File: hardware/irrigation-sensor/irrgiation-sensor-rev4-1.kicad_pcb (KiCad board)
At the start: 2 copper layers, 180 x 38 mm, 39 parts, among them J1 CONUFL001-SMD-T, J2 SHF-105-01-L-D-TH, Q1 TSM260P02, Q2 PMV250EPEA, U1 24LC32, U2 RFM95W, U3 STM32L412KB, U4 TLV61225, Y1 32768Hz

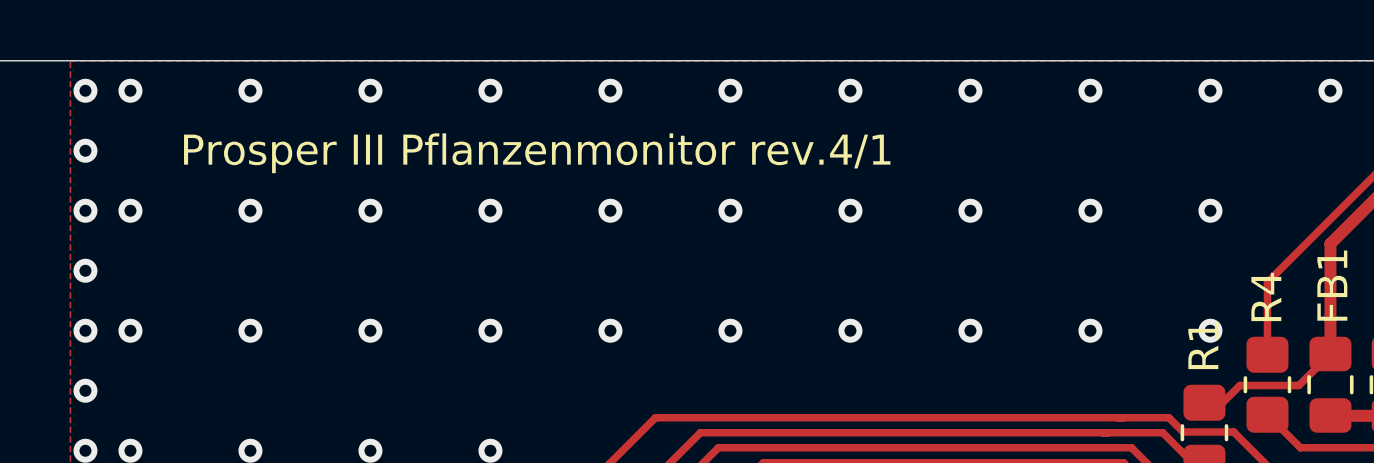
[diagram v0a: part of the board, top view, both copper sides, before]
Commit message: Add different irrigation sensor hardware revisions and cypress e2e tests
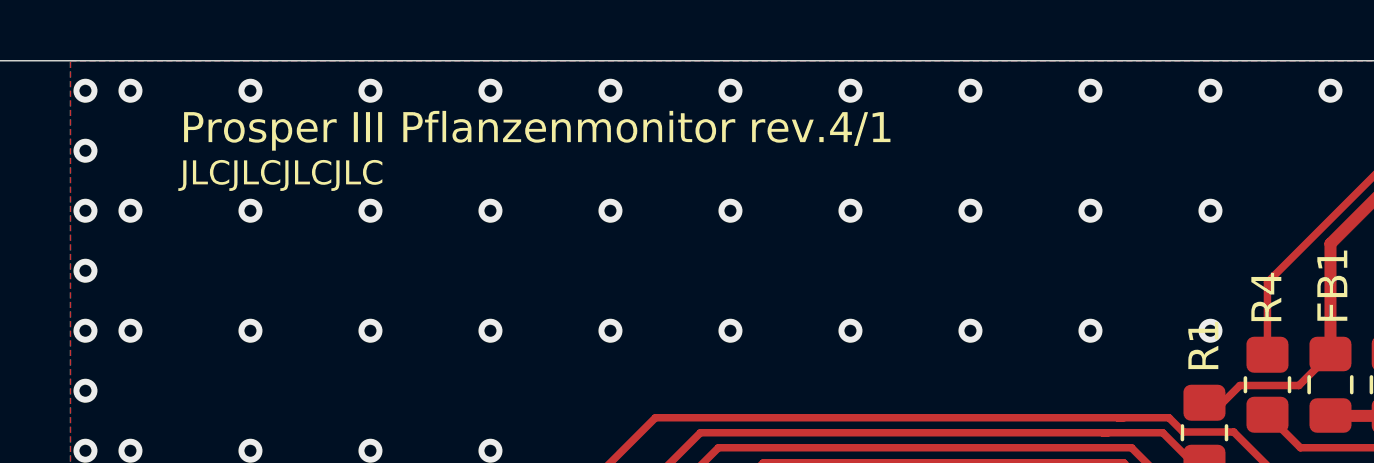
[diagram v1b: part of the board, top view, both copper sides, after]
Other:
- board text added: "JLCJLCJLCJLC"
